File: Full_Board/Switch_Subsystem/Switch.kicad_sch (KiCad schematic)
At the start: 7 parts, among them U7 JS102011SCQN, U8 UCLAMP3301H.TCT

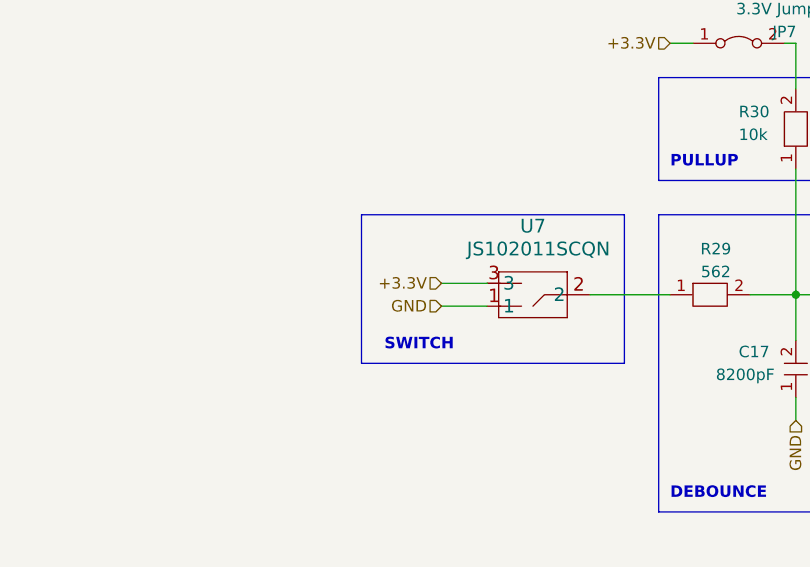
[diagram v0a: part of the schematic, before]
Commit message: Layed out the user buttons
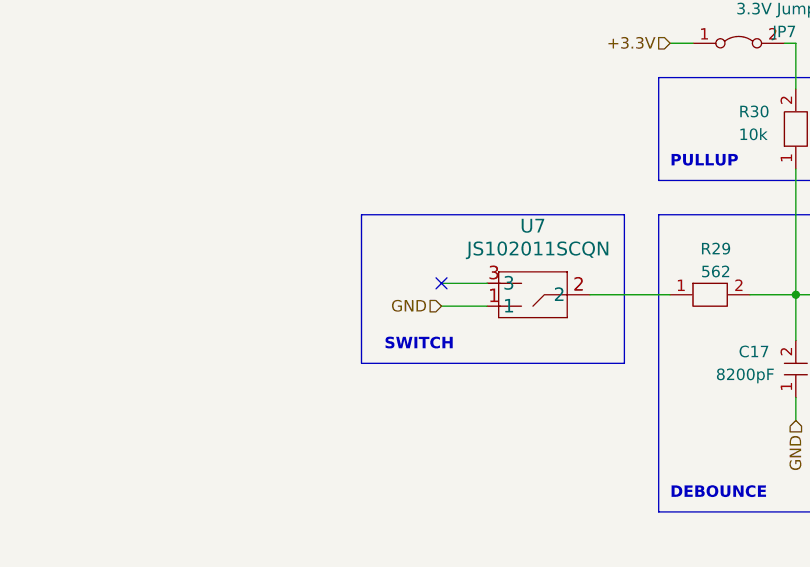
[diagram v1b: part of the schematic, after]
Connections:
- net +3.3V: no longer U7.3
- no-connect marks 0 -> 1
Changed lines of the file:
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@@
   (junction (at 137.16 93.98) (diameter 0) (color 0 0 0 0)
   )
+  (no_connect (at 97.79 92.71))
   (polyline (pts (xy 118.11 101.6) (xy 118.11 85.09))
     (stroke (width 0) (type default) (color 0 0 0 0))
@@
     (effects (font (size 1.27 1.27) bold) (justify left bottom))
   )
-  (hierarchical_label "+3.3V" (shape input) (at 97.79 92.71 180)
-    (effects (font (size 1.27 1.27)) (justify right))
-  )
   (hierarchical_label "GND" (shape input) (at 97.79 95.25 180)
